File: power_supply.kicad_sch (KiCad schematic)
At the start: 5 parts, among them U7 TPS613221A_SOT-23-5

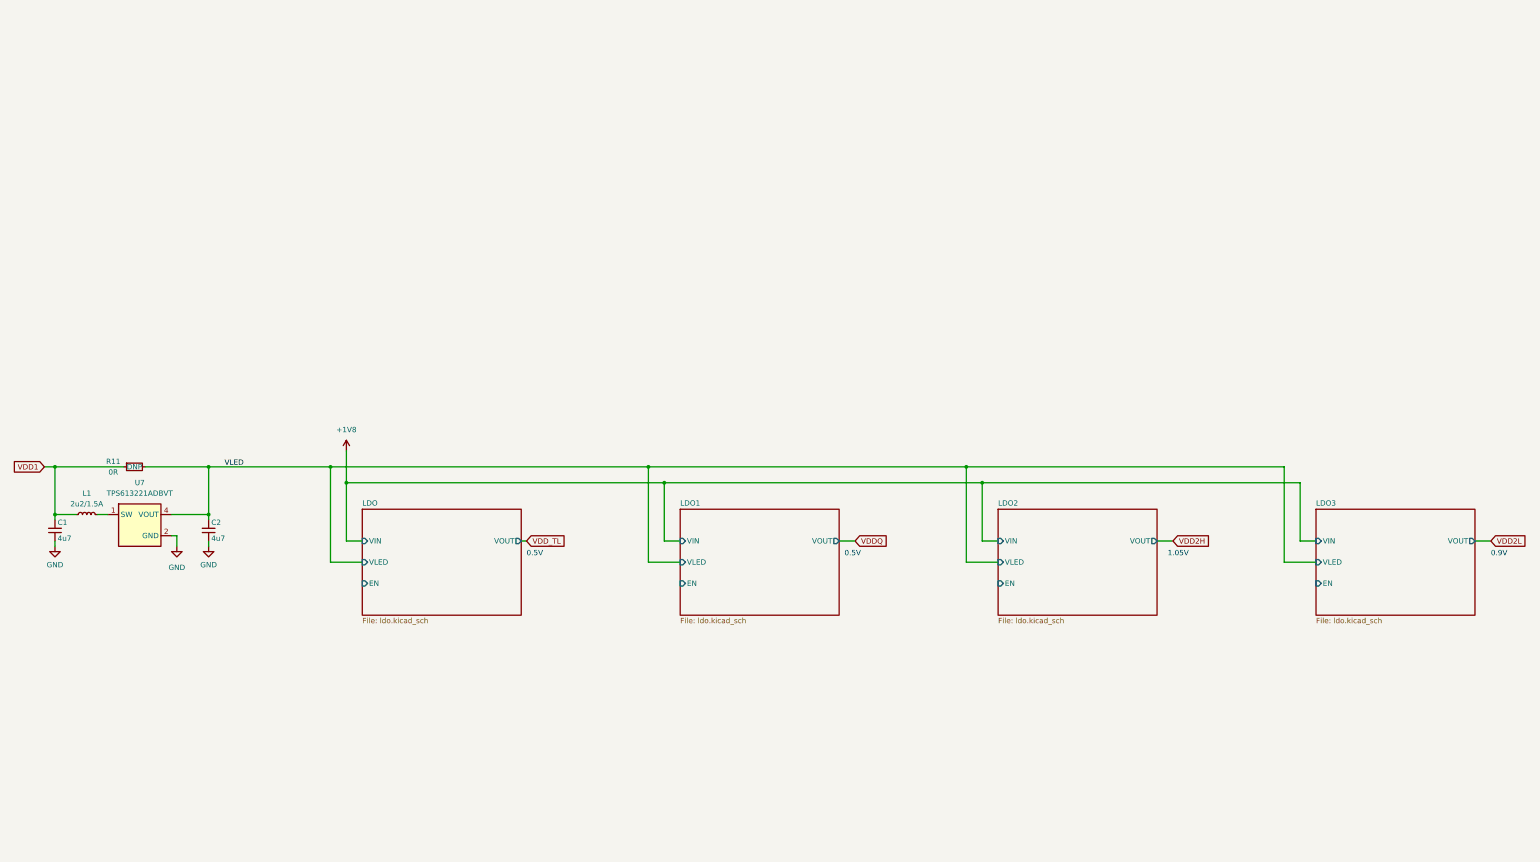
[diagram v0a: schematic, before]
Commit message: [#52835] schematics: add MPM54304GMN to Power Supply, update sheet
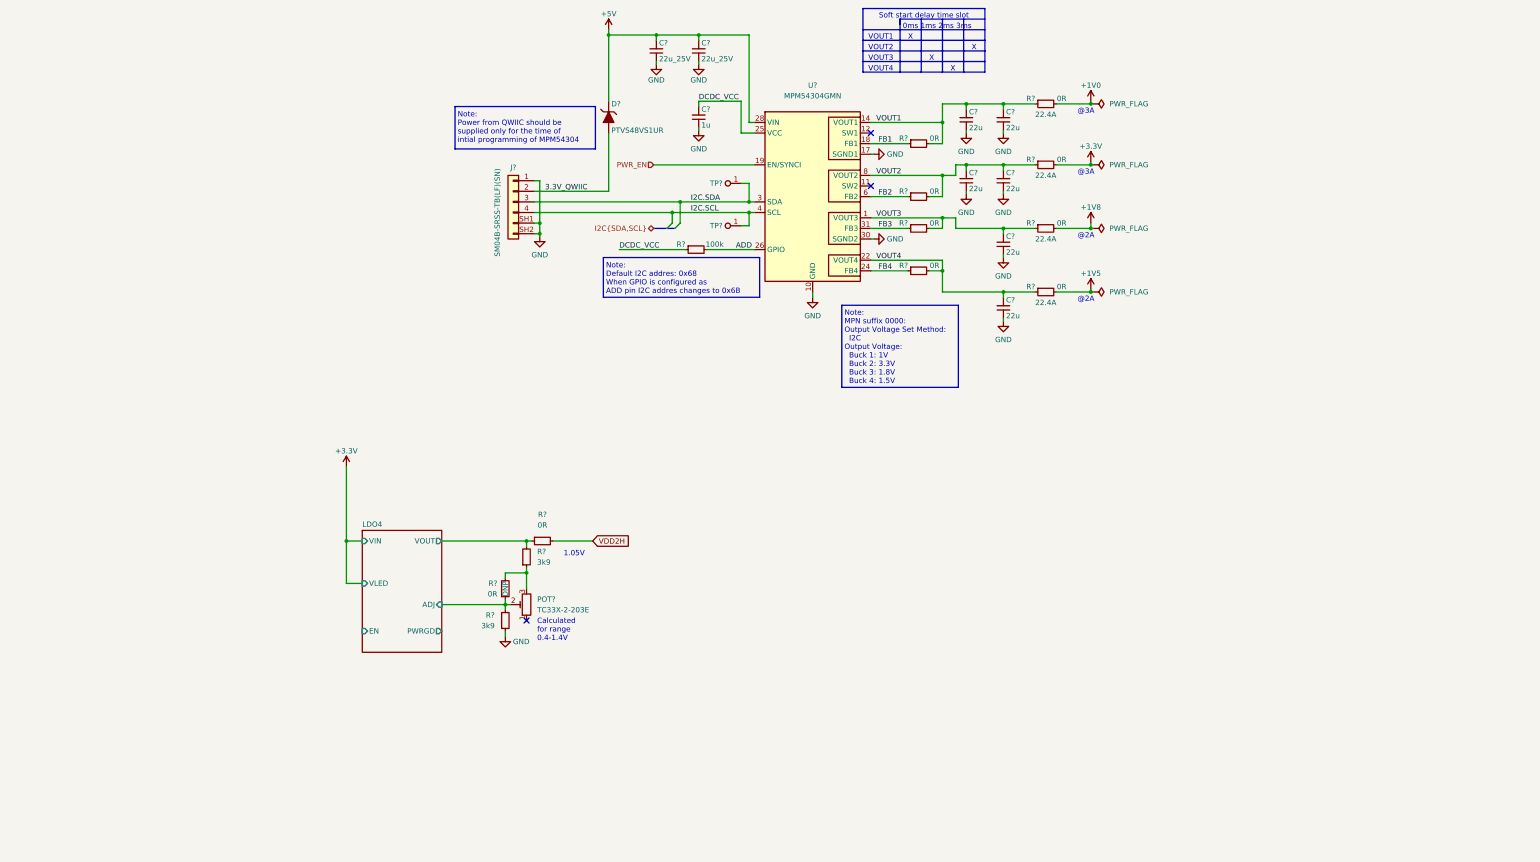
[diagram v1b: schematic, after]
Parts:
- removed C1, C2: C_4u7_0402, antmicro-footprints:C_0402_1005Metric, symbol antmicroCapacitors0402:C_4u7_0402
- removed L1: L_2u2_1.5A_0806, antmicro-footprints:L_0806_2016Metric, symbol antmicroFixedInductors:L_2u2_1.5A_0806
- removed R11: R_0R_0402, antmicro-footprints:R_0402_1005Metric, symbol antmicroResistors0402:R_0R_0402
- removed U7: TPS613221A_SOT-23-5, antmicro-footprints:SOT-23-5, symbol antmicroDCDCConverters:TPS613221A_SOT-23-5
- added C? (x6): C_22u_0603, antmicro-footprints:C_0603_1608Metric, symbol antmicroCapacitors0603:C_22u_0603
- added C? (x2): C_22u_25V_0805, antmicro-footprints:C_0805_2012Metric, symbol antmicroCapacitorsmisc:C_22u_25V_0805
- added C?: C_1u_0402, antmicro-footprints:C_0402_1005Metric, symbol antmicroCapacitors0402:C_1u_0402
- added D?: PTVS48VS1UR, antmicro-footprints:D_SOD-123F, symbol antmicroDiodesRectifiersSingle:PTVS48VS1UR
- added J?: JST_SH_1x4_SM04B-SRSS-TB-LF-SN, antmicro-footprints:Conn_JST_SH_1x4_SM04B-SRSS-TB-LF-SN, symbol antmicroWire2BoardConnectors:JST_SH_1x4_SM04B-SRSS-TB-LF-SN
- added POT?: TC33X-2-203E, antmicro-footprints:Trimpot_3.8mmx3.6mm_TC33X-2-103E, symbol antmicroTrimmerPotentiometers:TC33X-2-203E
- added R? (x2): R_3k9_0402, antmicro-footprints:R_0402_1005Metric, symbol antmicroResistors0402:R_3k9_0402
- added R? (x4): R_0R_22.4A_0603, antmicro-footprints:R_0603_1608Metric, symbol antmicroResistors0603:R_0R_22.4A_0603
- added R?: R_100k_0402, antmicro-footprints:R_0402_1005Metric, symbol antmicroResistors0402:R_100k_0402
- added R? (x6): R_0R_0402, antmicro-footprints:R_0402_1005Metric, symbol antmicroResistors0402:R_0R_0402
- added TP? (x2): TP_1mm_SMD, antmicro-footprints:TP_SMD_1mm, symbol antmicroTestPoints:TP_1mm_SMD
- added U?: MPM54304GMN, antmicro-footprints:MPS_LGA-33, symbol antmicroPMICVoltageRegulatorsDCDCSwitchingRegulators:MPM54304GMN
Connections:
- net +1V8: now also R?.2
- net GND: now also C?.1, C?.1, C?.1, C?.1, C?.1, C?.1, C?.1, C?.1, C?.1, J?.1, J?.SH1, J?.SH2, R?.1, U?.10 (GND), U?.13 (GND), U?.16 (GND), U?.17 (SGND1), U?.2 (GND), U?.20 (GND), U?.21 (GND), U?.27 (GND), U?.30 (SGND2), U?.33 (GND), U?.5 (GND), U?.7 (GND)
- net VDD2H: now also R?.2
- new net: POT?.3, R?.1, R?.2
- new net +1V0: R?.2
- new net +1V5: R?.2
- new net +3V3: R?.2
- new net +5V: C?.2, C?.2, D?.K (C), U?.28 (VIN), U?.29 (VIN)
- new net 3.3V_QWIIC: D?.A, J?.2
- new net ADD: R?.2, U?.26 (GPIO)
- new net DCDC_VCC: C?.2, R?.1, U?.25 (VCC)
- new net FB1: R?.1, U?.18 (FB1)
- new net FB2: R?.1, U?.6 (FB2)
- new net FB3: R?.1, U?.31 (FB3)
- new net FB4: R?.1, U?.24 (FB4)
- new net I2C.SCL: J?.4, TP?.1, U?.4 (SCL)
- new net I2C.SDA: J?.3, TP?.1, U?.3 (SDA)
- new net LDO4/ADJ: POT?.2, R?.1, R?.2
- new net LDO4/VOUT: R?.1, R?.2
- new net PWR_EN: U?.19 (EN/SYNCI)
- new net VOUT1: C?.2, C?.2, R?.1, R?.2, U?.14 (VOUT1), U?.15 (VOUT1)
- new net VOUT2: C?.2, C?.2, R?.1, R?.2, U?.8 (VOUT2), U?.9 (VOUT2)
- new net VOUT3: C?.2, R?.1, R?.2, U?.1 (VOUT3), U?.32 (VOUT3)
- new net VOUT4: C?.2, R?.1, R?.2, U?.22 (VOUT4), U?.23 (VOUT4)
- no-connect marks 0 -> 3
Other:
- removed sheet LDO
- removed sheet LDO1
- removed sheet LDO2
- removed sheet LDO3
- added sheet LDO4 (ldo.kicad_sch)
- note added: "0ms 1ms 2ms 3ms"
- note added: "@2A"
- note added: "@3A"
- note added: "Calculated for range 0.4-1.4V"
- note added: "Note: Default I2C addres: 0x68 When GPIO is configured as ADD pin I2C addres changes to 0x6B"
- note added: "Note: MPN suffix 0000: Output Voltage Set Method: I2C Output Voltage: Buck 1: 1V Buck 2: 3.3V Buck 3: 1.8V Buck 4: 1.5V"
- note added: "Note: Power from QWIIC should be supplied only for the time of intial programming of MPM54304"
- note added: "Soft start delay time slot"
- note added: "VOUT1"
- note added: "VOUT2"
- note added: "VOUT3"
- note added: "VOUT4"
- note added: "X"
- note removed: "0.5V"
- note removed: "0.9V"

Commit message: [#52835] schematics: update power supply section
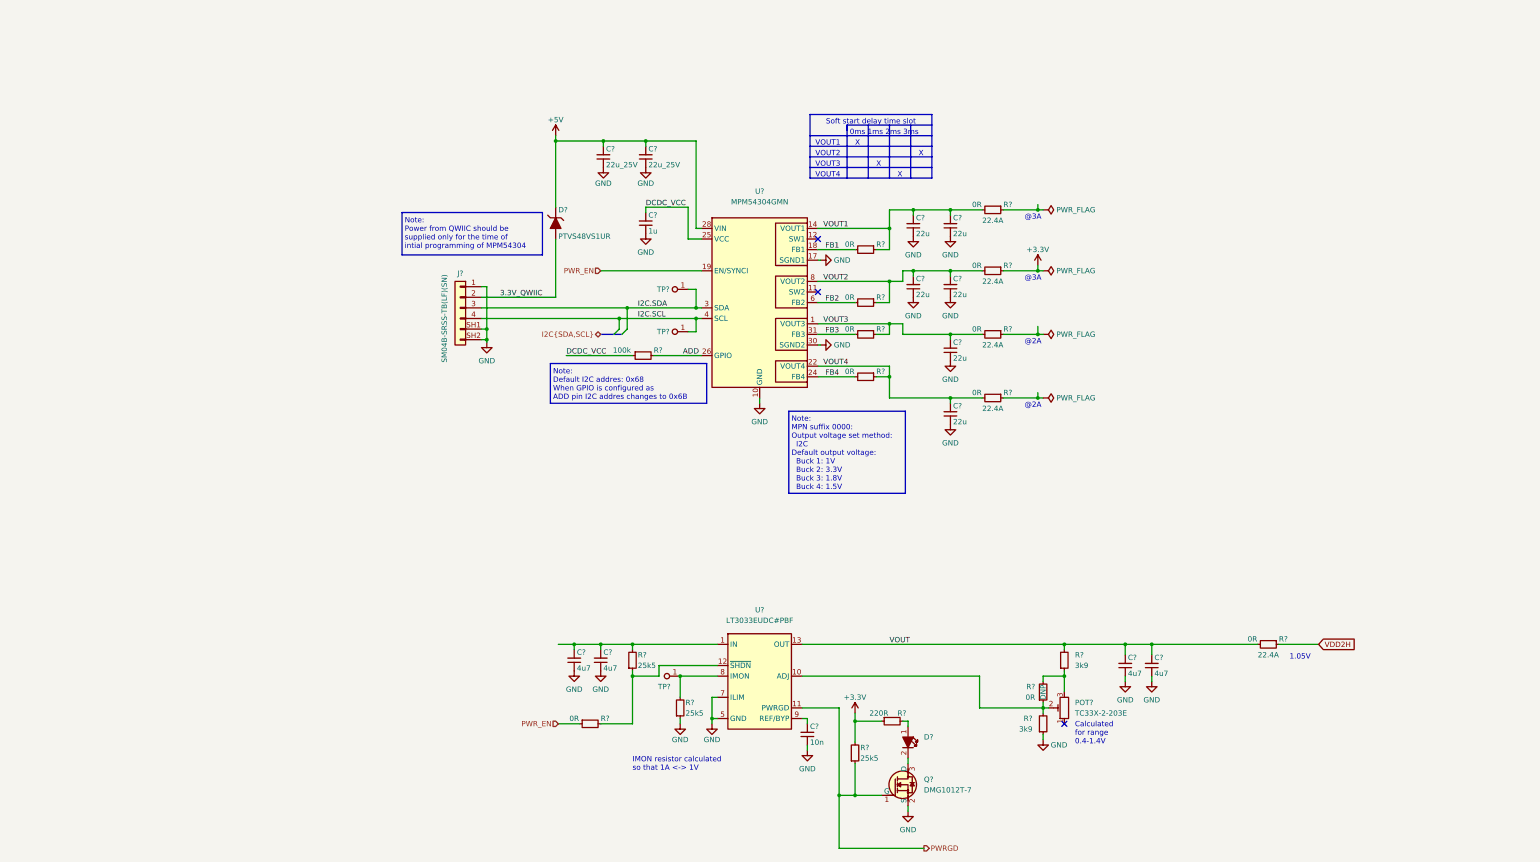
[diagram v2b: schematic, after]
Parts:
- removed R?: R_0R_0402, antmicro-footprints:R_0402_1005Metric, symbol antmicroResistors0402:R_0R_0402
- added C? (x4): C_4u7_0402, antmicro-footprints:C_0402_1005Metric, symbol antmicroCapacitors0402:C_4u7_0402
- added C?: C_10n_0402, antmicro-footprints:C_0402_1005Metric, symbol antmicroCapacitors0402:C_10n_0402
- added D?: LED_G_0603_KP-1608CGCK, antmicro-footprints:LED_0603_1608Metric_G, symbol antmicroLEDIndicationDiscrete:LED_G_0603_KP-1608CGCK
- added Q?: DMG1012T-7, antmicro-footprints:SOT-523, symbol antmicroTransistorsFETsMOSFETsSingle:DMG1012T-7
- added R?: R_220R_0402, antmicro-footprints:R_0402_1005Metric, symbol antmicroResistors0402:R_220R_0402
- added R? (x3): R_25k5_0402, antmicro-footprints:R_0402_1005Metric, symbol antmicroResistors0402:R_25k5_0402
- added R?: R_0R_0402, antmicro-footprints:R_0402_1005Metric, symbol antmicroResistors0402:R_0R_0402
- added R?: R_0R_22.4A_0603, antmicro-footprints:R_0603_1608Metric, symbol antmicroResistors0603:R_0R_22.4A_0603
- added TP?: TP_0.75mm_SMD, antmicro-footprints:TP_SMD_0.75mm, symbol antmicroTestPoints:TP_0.75mm_SMD
- added U?: LT3033EUDC_QFN, antmicro-footprints:QFN-20-4EP_3x4x0.75mm_P0.5mm_Layout4x6_LT3033, symbol antmicroPMICVoltageRegulatorsLinear:LT3033EUDC_QFN
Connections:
- net +1V0 is gone; now on net VOUT1: R?.2
- net +1V5 is gone; now on net VOUT4: R?.2
- net +1V8 is gone; now on net VOUT3: R?.2
- net +3V3: now also R?.1, R?.1, R?.2; no longer R?.2
- net FB1: now also R?.2; no longer R?.1
- net FB2: now also R?.2; no longer R?.1
- net FB3: now also R?.2; no longer R?.1
- net FB4: now also R?.2; no longer R?.1
- net GND: now also C?.1, C?.1, C?.1, C?.1, C?.1, Q?.2 (S), R?.1, U?.5 (GND), U?.6 (GND), U?.7 (ILIM)
- net PWR_EN: now also R?.1
- net VDD2H: now also R?.1
- net VOUT1: now also R?.1; no longer R?.1, R?.2
- net VOUT2: now also R?.1, R?.2; no longer R?.1, R?.2
- net VOUT3: now also R?.1; no longer R?.1, R?.2
- net VOUT4: now also R?.1; no longer R?.1, R?.2
- net LDO4/ADJ: no longer names the net of POT?.2, R?.1, R?.2
- net LDO4/ADJ: now also U?.10 (ADJ)
- net LDO4/VOUT renamed VOUT
- net VOUT: now also C?.2, C?.2, R?.2, U?.13 (OUT), U?.14 (OUT), U?.17 (OUT), U?.18 (OUT), U?.19 (OUT), U?.20 (OUT), U?.23 (OUT), U?.24 (OUT), U?.3 (OUT), U?.4 (OUT)
- new net: C?.2, C?.2, R?.2, U?.1 (IN), U?.15 (IN), U?.16 (IN), U?.2 (IN), U?.21 (IN), U?.22 (IN)
- new net: D?.1, R?.2
- new net: C?.2, U?.9 (REF/BYP)
- new net: R?.1, R?.2, U?.12 (~{SHDN})
- new net: R?.2, TP?.1, U?.8 (IMON)
- new net: D?.2, Q?.3 (D)
- new net PWRGD: Q?.1 (G), R?.1, U?.11 (PWRGD)
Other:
- removed sheet LDO4
- note added: "IMON resistor calculated so that 1A <-> 1V"
- note added: "Note: MPN suffix 0000: Output voltage set method: I2C Default output voltage: Buck 1: 1V Buck 2: 3.3V Buck 3: 1.8V Buck 4: 1.5V"
- note removed: "Note: MPN suffix 0000: Output Voltage Set Method: I2C Output Voltage: Buck 1: 1V Buck 2: 3.3V Buck 3: 1.8V Buck 4: 1.5V"
- moved on the sheet: C?, D?, J?, POT?, R?, TP?, U?

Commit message: [#52536] schematics: setup resistor dividers for DCDC converter
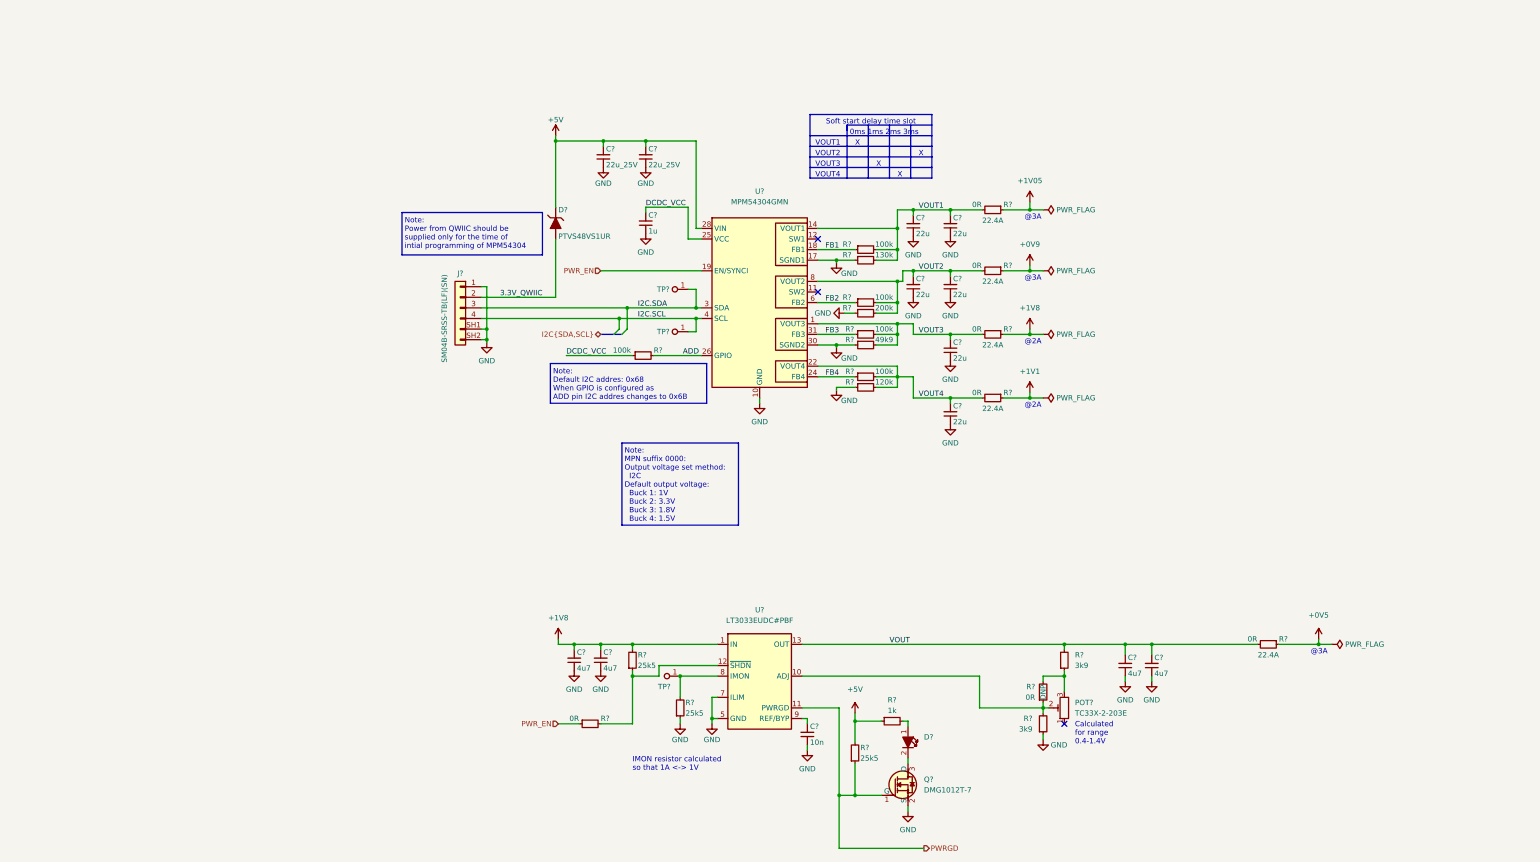
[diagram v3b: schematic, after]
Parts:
- removed R?: R_220R_0402, antmicro-footprints:R_0402_1005Metric, symbol antmicroResistors0402:R_220R_0402
- removed R? (x4): R_0R_0402, antmicro-footprints:R_0402_1005Metric, symbol antmicroResistors0402:R_0R_0402
- added R?: R_49k9_0402, antmicro-footprints:R_0402_1005Metric, symbol antmicroResistors0402:R_49k9_0402
- added R? (x4): R_100k_0402, antmicro-footprints:R_0402_1005Metric, symbol antmicroResistors0402:R_100k_0402
- added R?: R_130k_0402, antmicro-footprints:R_0402_1005Metric, symbol antmicroResistors0402:R_130k_0402
- added R?: R_200k_0402, antmicro-footprints:R_0402_1005Metric, symbol antmicroResistors0402:R_200k_0402
- added R?: R_120k_0402, antmicro-footprints:R_0402_1005Metric, symbol antmicroResistors0402:R_120k_0402
- added R?: R_1k_0402, antmicro-footprints:R_0402_1005Metric, symbol antmicroResistors0402:R_1k_0402
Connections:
- net +5V: now also R?.2, R?.1
- net FB1: now also R?.1
- net FB2: now also R?.1
- net FB3: now also R?.1
- net FB4: now also R?.1
- net GND: now also R?.1, R?.1, R?.1, R?.1
- net VOUT1: now also R?.2, R?.2
- net VOUT2: now also R?.2, R?.2
- net VOUT3: now also R?.2, R?.2
- net VOUT4: now also R?.2, R?.2
- net +1V8: now reaches C?.2, C?.2, R?.2, U?.1 (IN), U?.15 (IN), U?.16 (IN), U?.2 (IN), U?.21 (IN), U?.22 (IN)
- net +1V8: now also R?.1
- net at D?.1: now also R?.2
- net +1V1: now reaches R?.1
- net +1V05: now reaches R?.1
- net +3V3 renamed +0V9
- net +0V9: no longer R?.2
- net VDD2H renamed +0V5
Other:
- note removed: "1.05V"
